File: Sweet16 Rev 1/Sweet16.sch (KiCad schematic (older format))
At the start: 69 parts, among them J1 Conn_01x09_Male, J10 SW_half_inverter, J11 R_clock, J12 OUT_clock, J13 SW_dual8_hex, J14 OUT_OUT, J15 R_sync_pitch_1, J16 SW_sync_1, J17 R_sync_pitch_2, J18 SW_sync_2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

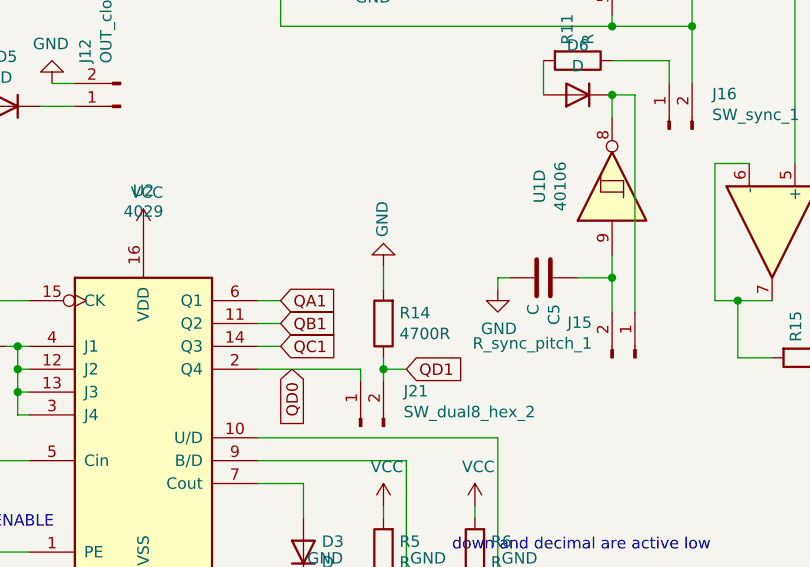
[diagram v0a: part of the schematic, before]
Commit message: Revert "moved the pulldown where it would work"
This reverts commit ad45cd7af2cd5e29d93eb6355ad2eb9f66b6a434.
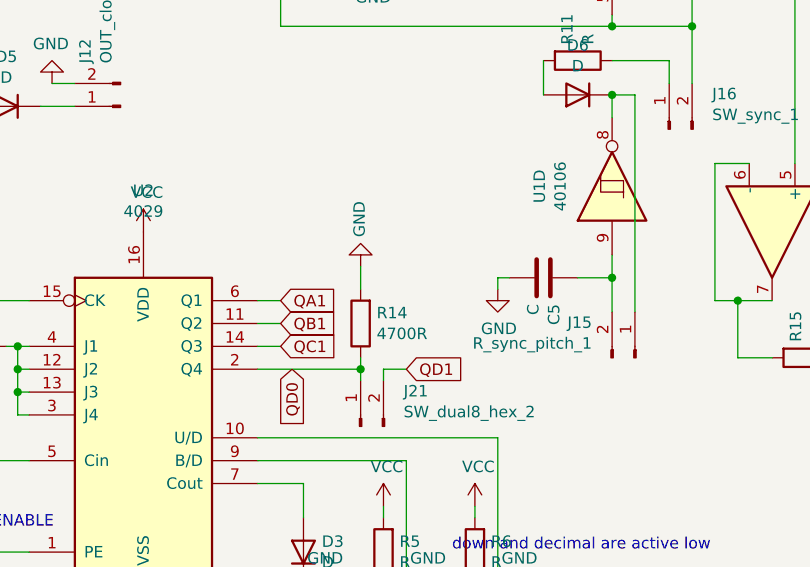
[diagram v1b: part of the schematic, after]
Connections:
- net QD0: now also R14.1
- net QD1: no longer R14.1
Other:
- moved on the sheet: R14
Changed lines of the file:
@@
 L Device:R R14
 U 1 1 61125FE1
-P 4000 6250
-F 0 "R14" H 3930 6204 50  0000 R CNN
-F 1 "4700R" H 3930 6295 50  0000 R CNN
-F 2 "Resistor_THT:R_Axial_DIN0207_L6.3mm_D2.5mm_P7.62mm_Horizontal" V 3930 6250 50  0001 C CNN
-F 3 "~" H 4000 6250 50  0001 C CNN
-	1    4000 6250
+P 3900 6250
+F 0 "R14" H 3830 6204 50  0000 R CNN
+F 1 "4700R" H 3830 6295 50  0000 R CNN
+F 2 "Resistor_THT:R_Axial_DIN0207_L6.3mm_D2.5mm_P7.62mm_Horizontal" V 3830 6250 50  0001 C CNN
+F 3 "~" H 3900 6250 50  0001 C CNN
+	1    3900 6250
 	-1   0    0    1
 $EndComp
@@
 	3450 6450 3900 6450
 Wire Wire Line
-	4000 6450 4000 6400
+	3900 6450 3900 6400
 Wire Wire Line
 	3900 6500 3900 6450
+Connection ~ 3900 6450
 $Comp
 L power:GND #PWR0141
 U 1 1 61145C06
-P 4000 6000
-F 0 "#PWR0141" H 4000 5750 50  0001 C CNN
-F 1 "GND" V 4005 5872 50  0000 R CNN
-F 2 "" H 4000 6000 50  0001 C CNN
-F 3 "" H 4000 6000 50  0001 C CNN
-	1    4000 6000
+P 3900 6000
+F 0 "#PWR0141" H 3900 5750 50  0001 C CNN
+F 1 "GND" V 3905 5872 50  0000 R CNN
+F 2 "" H 3900 6000 50  0001 C CNN
+F 3 "" H 3900 6000 50  0001 C CNN
+	1    3900 6000
 	-1   0    0    1
 $EndComp
 Wire Wire Line
-	4000 6100 4000 6000
+	3900 6100 3900 6000
 Wire Wire Line
 	4000 6500 4000 6450
@@
 Text GLabel 3600 6450 3    50   Input ~ 0
 QD0
-Connection ~ 4000 6450
 $EndSCHEMATC

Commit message: fixed pulldown AND kept all buzzard labels
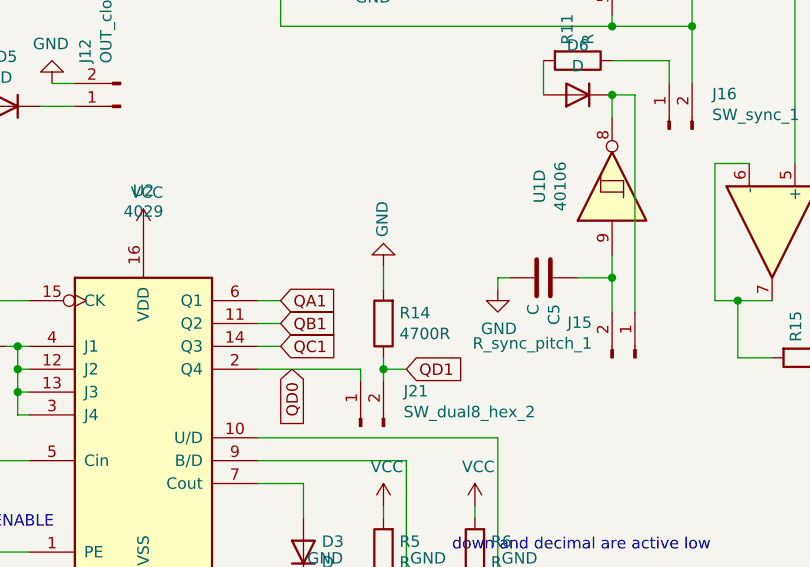
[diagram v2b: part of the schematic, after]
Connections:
- net QD0: no longer R14.1
- net QD1: now also R14.1
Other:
- moved on the sheet: R14
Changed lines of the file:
@@
 L Device:R R14
 U 1 1 61125FE1
-P 3900 6250
-F 0 "R14" H 3830 6204 50  0000 R CNN
-F 1 "4700R" H 3830 6295 50  0000 R CNN
-F 2 "Resistor_THT:R_Axial_DIN0207_L6.3mm_D2.5mm_P7.62mm_Horizontal" V 3830 6250 50  0001 C CNN
-F 3 "~" H 3900 6250 50  0001 C CNN
-	1    3900 6250
+P 4000 6250
+F 0 "R14" H 3930 6204 50  0000 R CNN
+F 1 "4700R" H 3930 6295 50  0000 R CNN
+F 2 "Resistor_THT:R_Axial_DIN0207_L6.3mm_D2.5mm_P7.62mm_Horizontal" V 3930 6250 50  0001 C CNN
+F 3 "~" H 4000 6250 50  0001 C CNN
+	1    4000 6250
 	-1   0    0    1
 $EndComp
@@
 	3450 6450 3900 6450
 Wire Wire Line
-	3900 6450 3900 6400
+	4000 6450 4000 6400
 Wire Wire Line
 	3900 6500 3900 6450
-Connection ~ 3900 6450
 $Comp
 L power:GND #PWR0141
 U 1 1 61145C06
-P 3900 6000
-F 0 "#PWR0141" H 3900 5750 50  0001 C CNN
-F 1 "GND" V 3905 5872 50  0000 R CNN
-F 2 "" H 3900 6000 50  0001 C CNN
-F 3 "" H 3900 6000 50  0001 C CNN
-	1    3900 6000
+P 4000 6000
+F 0 "#PWR0141" H 4000 5750 50  0001 C CNN
+F 1 "GND" V 4005 5872 50  0000 R CNN
+F 2 "" H 4000 6000 50  0001 C CNN
+F 3 "" H 4000 6000 50  0001 C CNN
+	1    4000 6000
 	-1   0    0    1
 $EndComp
 Wire Wire Line
-	3900 6100 3900 6000
+	4000 6100 4000 6000
 Wire Wire Line
 	4000 6500 4000 6450
@@
 Text GLabel 3600 6450 3    50   Input ~ 0
 QD0
+Connection ~ 4000 6450
 $EndSCHEMATC
